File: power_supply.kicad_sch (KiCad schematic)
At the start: 9 parts, among them SW1 SW_Push, U1 STM32F401RBTx, Y1 26MHz

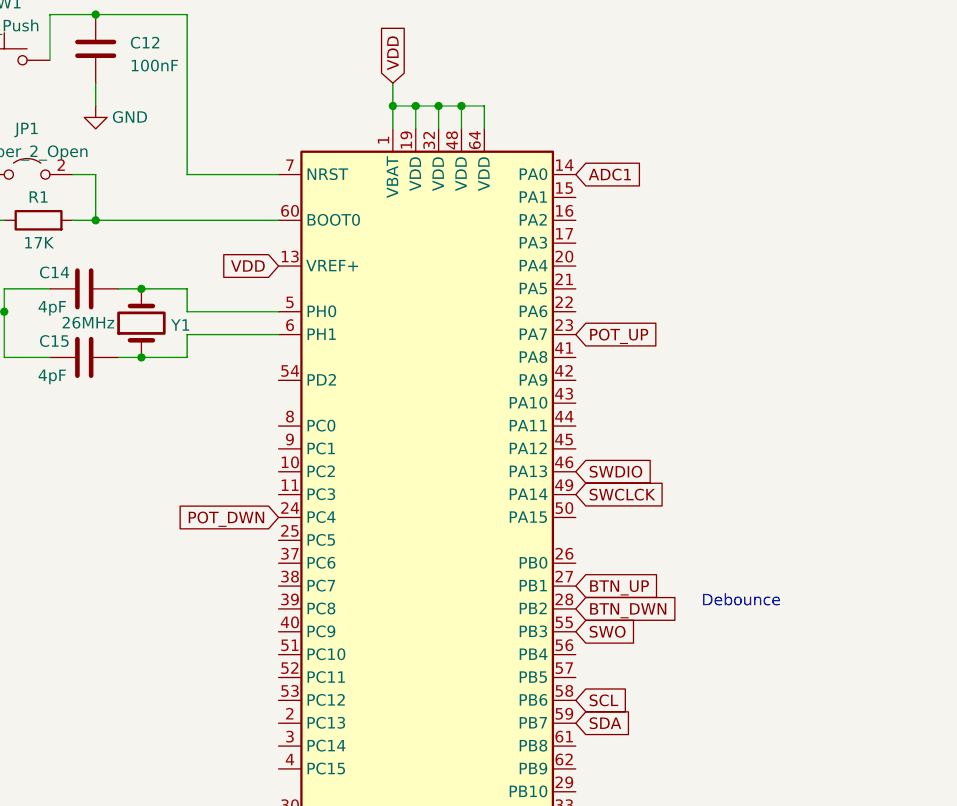
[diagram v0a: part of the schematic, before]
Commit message: Adjusted the VDD supply schematic
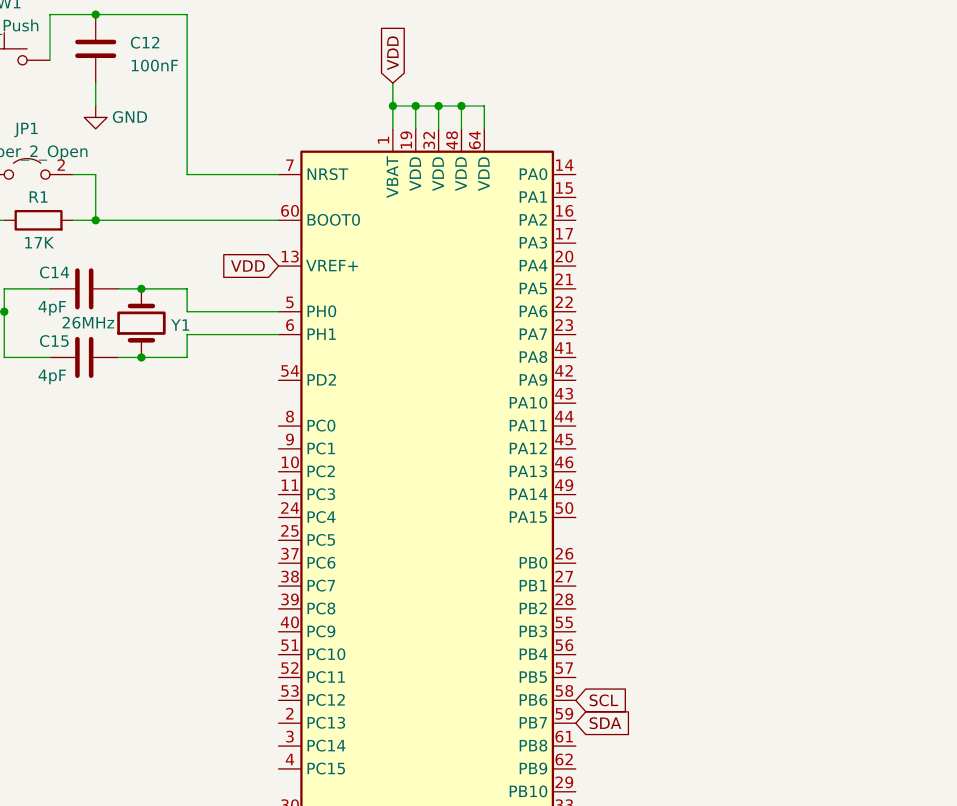
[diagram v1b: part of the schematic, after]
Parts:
- JP1: footprint TestPoint:TestPoint_Bridge_Pitch2.54mm_Drill0.7mm -> (none)
- SW1: footprint Button_Switch_THT:SW_PUSH_6mm_H7.3mm -> (none)
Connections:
- net ADC1: no longer names the net of U1.14 (PA0)
- net BTN_DWN: no longer names the net of U1.28 (PB2)
- net BTN_UP: no longer names the net of U1.27 (PB1)
- net POT_DWN: no longer names the net of U1.24 (PC4)
- net POT_UP: no longer names the net of U1.23 (PA7)
- net SWCLCK: no longer names the net of U1.49 (PA14)
- net SWDIO: no longer names the net of U1.46 (PA13)
- net SWO: no longer names the net of U1.55 (PB3)
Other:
- note removed: "Debounce"
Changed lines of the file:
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@@
     (fill (type none))
-  )
-  (text "Debounce" (at 181.61 127 0)
-    (effects (font (size 1.27 1.27)) (justify left bottom))
   )
   (text "Components\n" (at 140.462 48.768 0)
     (effects (font (size 2 2)) (justify left bottom))
-  )
-  (global_label "POT_UP" (shape input) (at 167.64 96.52 0) (fields_autoplaced)
-    (effects (font (size 1.27 1.27)) (justify left))
-    (property "Intersheetrefs" "${INTERSHEET_REFS}" (at 177.682 96.52 0)
-      (effects (font (size 1.27 1.27)) (justify left) hide)
-    )
   )
   (global_label "VDD" (shape input) (at 147.32 68.58 90) (fields_autoplaced)
@@
     )
   )
-  (global_label "SWO" (shape input) (at 167.64 129.54 0) (fields_autoplaced)
-    (effects (font (size 1.27 1.27)) (justify left))
-    (property "Intersheetrefs" "${INTERSHEET_REFS}" (at 174.5372 129.54 0)
-      (effects (font (size 1.27 1.27)) (justify left) hide)
-    )
-  )
-  (global_label "BTN_UP" (shape input) (at 167.64 124.46 0) (fields_autoplaced)
-    (effects (font (size 1.27 1.27)) (justify left))
-    (property "Intersheetrefs" "${INTERSHEET_REFS}" (at 177.682 124.46 0)
-      (effects (font (size 1.27 1.27)) (justify left) hide)
-    )
-  )
   (global_label "VDD" (shape input) (at 99.06 78.74 180) (fields_autoplaced)
     (effects (font (size 1.27 1.27)) (justify right))
@@
     )
   )
-  (global_label "ADC1" (shape input) (at 167.64 78.74 0) (fields_autoplaced)
-    (effects (font (size 1.27 1.27)) (justify left))
-    (property "Intersheetrefs" "${INTERSHEET_REFS}" (at 175.3839 78.74 0)
-      (effects (font (size 1.27 1.27)) (justify left) hide)
-    )
-  )
   (global_label "VDD" (shape input) (at 134.62 88.9 180) (fields_autoplaced)
     (effects (font (size 1.27 1.27)) (justify right))
     (property "Intersheetrefs" "${INTERSHEET_REFS}" (at 128.0856 88.9 0)
       (effects (font (size 1.27 1.27)) (justify right) hide)
-    )
-  )
-  (global_label "POT_DWN" (shape input) (at 134.62 116.84 180) (fields_autoplaced)
-    (effects (font (size 1.27 1.27)) (justify right))
-    (property "Intersheetrefs" "${INTERSHEET_REFS}" (at 123.1266 116.84 0)
-      (effects (font (size 1.27 1.27)) (justify right) hide)
-    )
-  )
-  (global_label "BTN_DWN" (shape input) (at 167.64 127 0) (fields_autoplaced)
-    (effects (font (size 1.27 1.27)) (justify left))
-    (property "Intersheetrefs" "${INTERSHEET_REFS}" (at 179.1334 127 0)
-      (effects (font (size 1.27 1.27)) (justify left) hide)
-    )
-  )
-  (global_label "SWCLCK" (shape input) (at 167.64 114.3 0) (fields_autoplaced)
-    (effects (font (size 1.27 1.27)) (justify left))
-    (property "Intersheetrefs" "${INTERSHEET_REFS}" (at 178.0448 114.3 0)
-      (effects (font (size 1.27 1.27)) (justify left) hide)
-    )
-  )
-  (global_label "SWDIO" (shape input) (at 167.64 111.76 0) (fields_autoplaced)
-    (effects (font (size 1.27 1.27)) (justify left))
-    (property "Intersheetrefs" "${INTERSHEET_REFS}" (at 176.412 111.76 0)
-      (effects (font (size 1.27 1.27)) (justify left) hide)
     )
   )
@@
       (effects (font (size 1.27 1.27)))
     )
-    (property "Footprint" "TestPoint:TestPoint_Bridge_Pitch2.54mm_Drill0.7mm" (at 106.68 78.74 0)
+    (property "Footprint" "" (at 106.68 78.74 0)
       (effects (font (size 1.27 1.27)) hide)
     )
@@
       (effects (font (size 1.27 1.27)))
     )
-    (property "Footprint" "Button_Switch_THT:SW_PUSH_6mm_H7.3mm" (at 104.14 60.96 0)
-      (effects (font (size 1.27 1.27)) hide)
-    )
+    (property "Footprint" "" (at 104.14 60.96 0)
+      (effects (font (size 1.27 1.27)) hide)
+    )
